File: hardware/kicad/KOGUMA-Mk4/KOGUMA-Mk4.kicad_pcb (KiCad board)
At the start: 2 copper layers, 75.6 x 69.2 mm, 143 parts, among them J1 BATT (BT2.0), J2 MOTOR_L, J3 MOTOR_R, J4 FAN, J5 ENC_L, J6 ENC_R, J7 DEBUG (STLINK-V3MODS), Q1 AO4407A, Q40 IRLML6344, Q90 2N7002, SW1 SSSS810701, SW2 TVAF06-A020B-R, U1 LXDC55FAAA-203, U2 MP6551GQB, U3 MP6551GQB, U4 STM32H725RGVx, U70 NJU6080, U71 NJU6080, U72 NJU6080, U73 NJU6080, U74 OPA2354, U75 OPA2354, U76 LSM6DSR, Y1 CSTNE10M0G52Z000R0

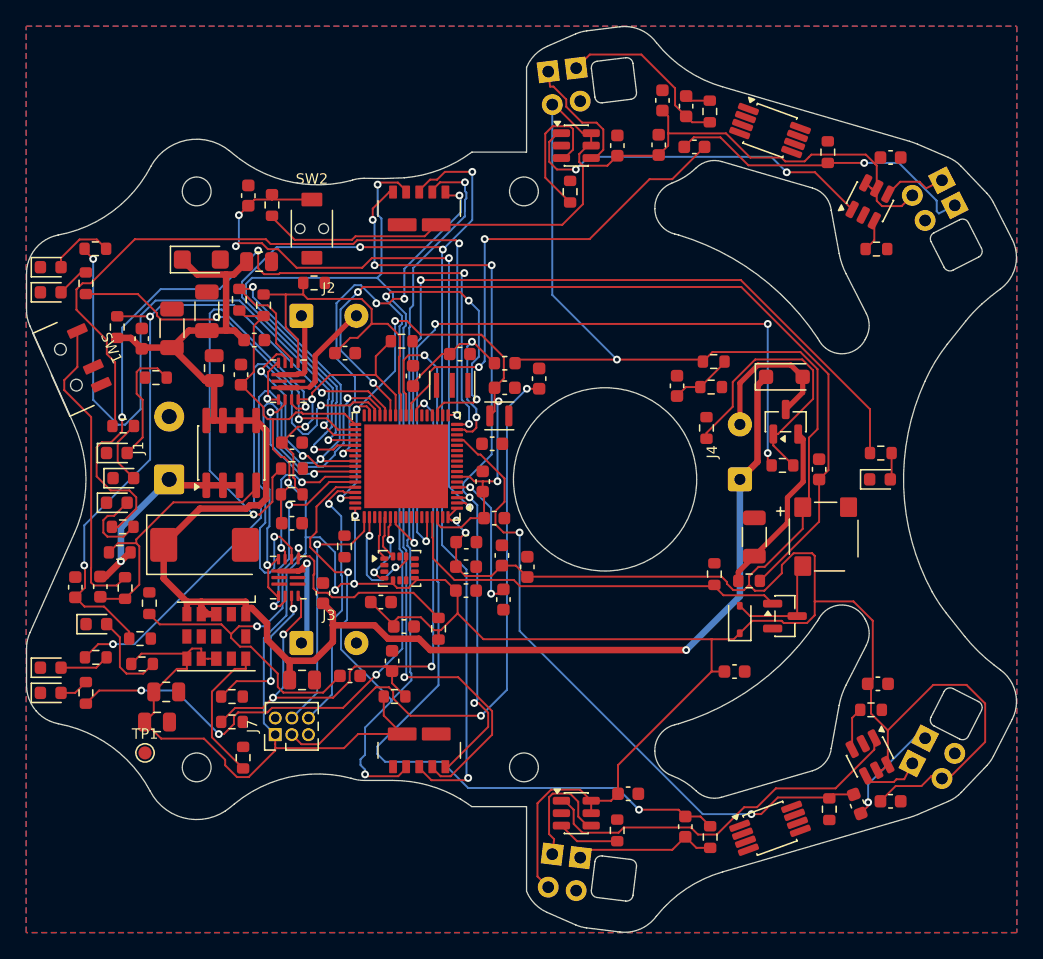
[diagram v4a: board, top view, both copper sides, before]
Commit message: 自動配線の5回目(1段目、GND なし): 穴のクリアランスの違反 0、縁の違反 3。GND 以外で残り 38 本
Co-Authored-By: Claude Opus 5.5 <noreply@anthropic.com>
Claude-Session: https://claude.ai/code/session_01H2Zvpqxqu2v63zaiCMmfT3
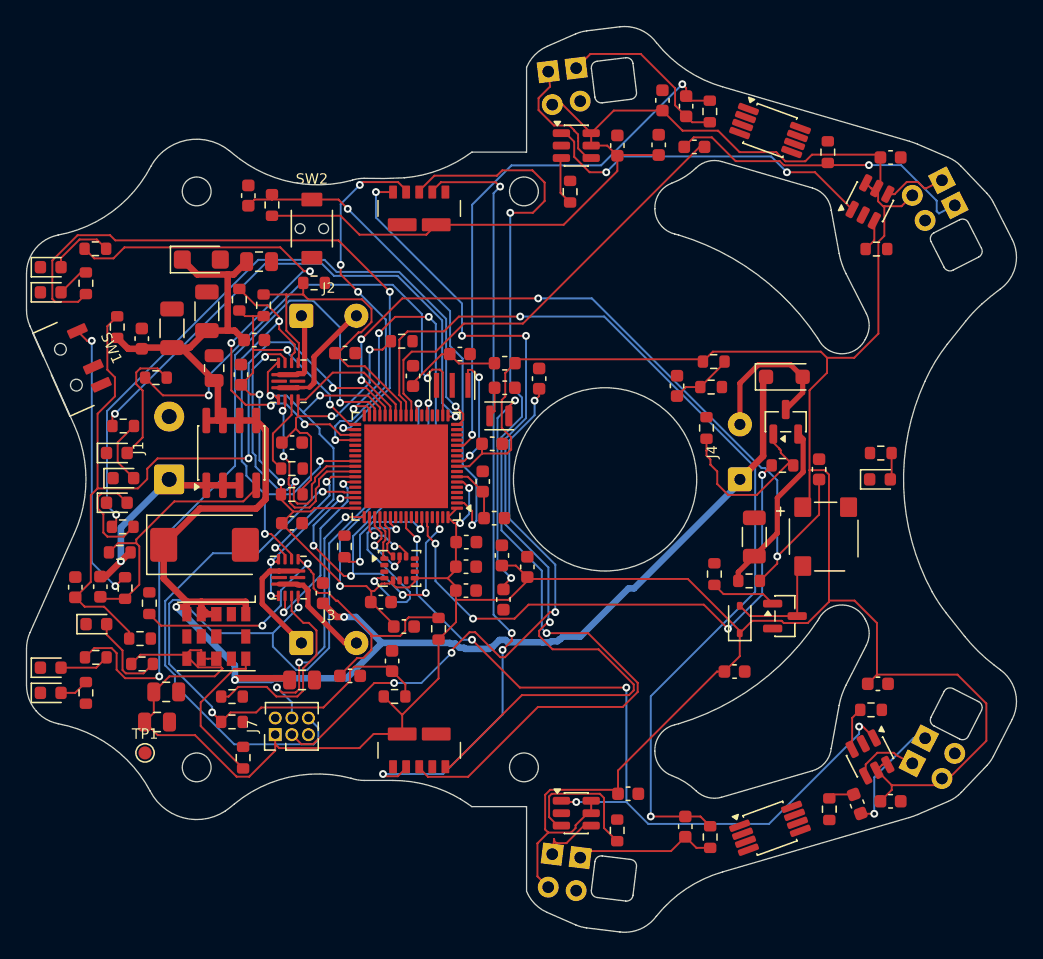
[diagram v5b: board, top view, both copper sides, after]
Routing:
- net LED_NUM0: track 75.3 -> 0.00 mm, vias 6 -> 0
- net LED_FRONT: track 64.7 -> 0.00 mm, vias 2 -> 0
- net ENC_MISO: track 84.8 -> 29.2 mm, vias 3 -> 4
- net WALL_L: track 50.3 -> 1.99 mm, vias 2 -> 0
- net WALL_FL: track 1.95 -> 42.0 mm, vias 0 -> 2
- net LED_MODE2: track 0.00 -> 37.1 mm, vias 0 -> 2
- net WALL_LED_L_FR: track 29.5 -> 62.3 mm, vias 0 -> 5
- net ENC_L_CS: track 31.0 -> 0.00 mm, vias 4 -> 0
- net Net-(U2-SR(6)): track 34.1 -> 6.13 mm, vias 2 -> 0
- net BUZZER: track 30.7 -> 5.04 mm
- net LED_NUM2: track 26.4 -> 47.4 mm
- net MOT_nFAULT: track 57.1 -> 37.5 mm
- net SWDIO: track 20.5 -> 39.7 mm
- net MOT_R_CM2: track 51.8 -> 70.4 mm, vias 4 -> 3
- net ENC_SCK: track 77.6 -> 60.3 mm, vias 3 -> 4
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- removed copper zone on B.Cu, net GND
- removed copper zone on F.Cu, net GND
